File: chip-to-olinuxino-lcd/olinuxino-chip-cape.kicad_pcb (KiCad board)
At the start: 2 copper layers, 41.9 x 64.8 mm, 4 parts, among them U1 LCD Olinuxino Connector, U13 LCD Connector, U14 Generic Connector

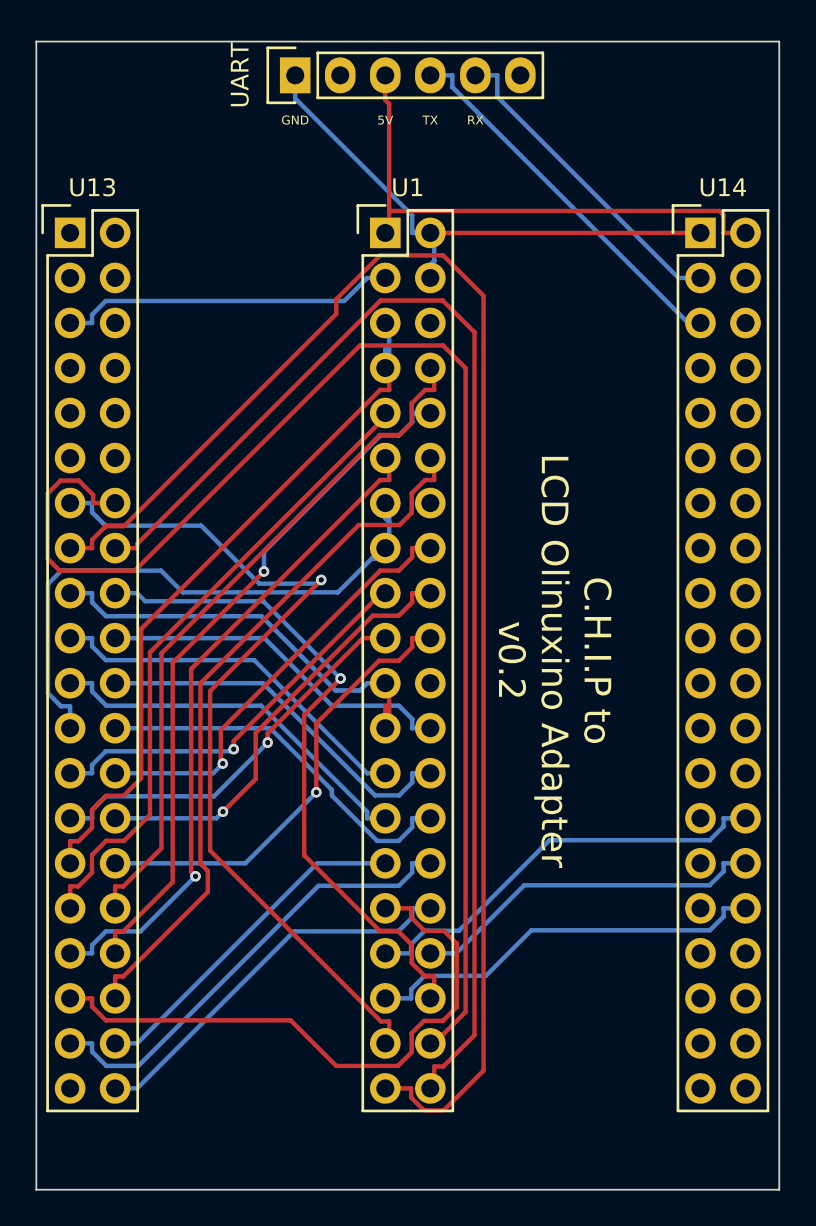
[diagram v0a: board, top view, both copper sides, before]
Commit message: rerouting
Signed-off-by: Maxime Ripard <maxime.ripard@free-electrons.com>
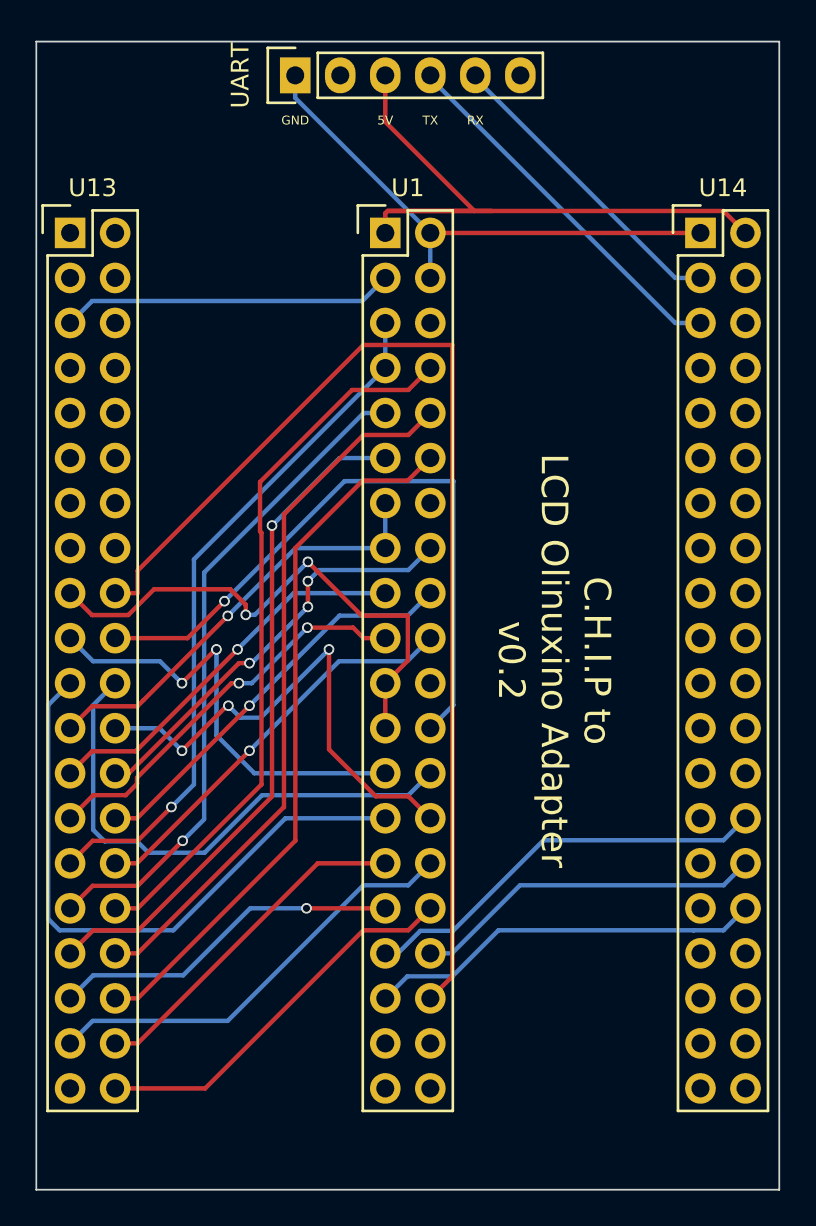
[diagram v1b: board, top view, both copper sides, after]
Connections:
- net /TPX1 renamed /TP_X-
- net /TPX2 renamed /TP_X+
- net /TPY1 renamed /TP_Y-
- net /TPY2 renamed /TP_Y+
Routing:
- net /TP_Y-: track 82.9 -> 0.22 mm
- net /TP_X+: track 78.0 -> 0.00 mm
- net /TP_Y+: track 71.5 -> 1.33 mm
- net /TP_X-: track 50.3 -> 1.76 mm, vias 1 -> 0
- net /PWM0: track 38.3 -> 64.3 mm, vias 1 -> 0
- net /LCD_D3: track 20.4 -> 37.4 mm, vias 0 -> 1
- net /LCD_CLK: track 34.4 -> 19.9 mm, vias 0 -> 1
- net /LCD_D6: track 21.6 -> 35.9 mm
- net /LCD_D10: track 34.9 -> 24.5 mm, vias 0 -> 1
- net /LCD_D5: track 21.4 -> 30.4 mm
- net /5V: track 30.9 -> 39.0 mm
- net /LCD_D7: track 21.7 -> 28.7 mm, vias 0 -> 3
- net /LCD_D2: track 25.0 -> 30.9 mm, vias 0 -> 2
- net /LCD_D4: track 21.4 -> 25.6 mm, vias 0 -> 2
- net /LCD_D15: track 25.8 -> 23.3 mm
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
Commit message: turn the connector around, and reroute
Signed-off-by: Maxime Ripard <maxime.ripard@free-electrons.com>
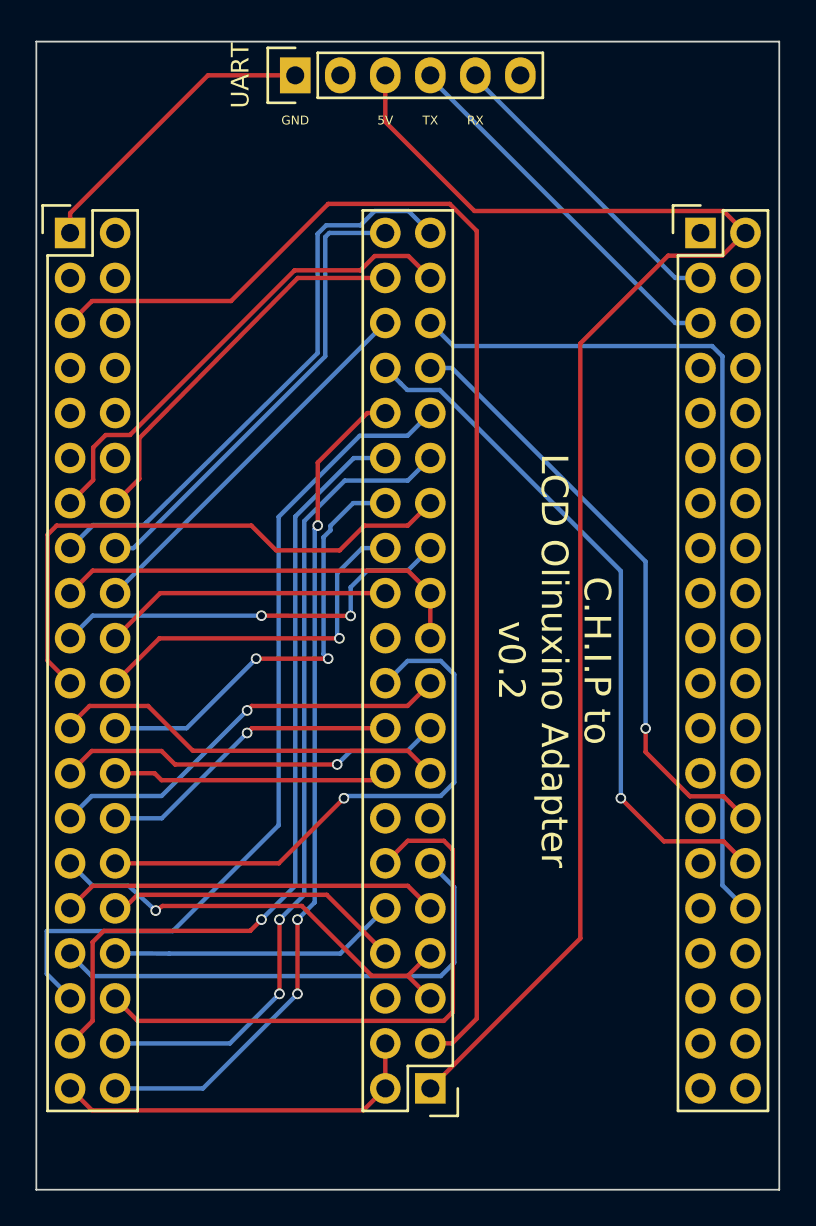
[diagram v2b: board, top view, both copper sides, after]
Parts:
- moved U1 48.3 mm to (152.3, 152.3), turned to 180 degrees
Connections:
- U1 pad 2: /GND -> /GND2
- U1 pad 4: /GND -> /GND2
- U13 pad 1: Net-(U13-Pad1) -> /GND
- U13 pad 39: Net-(U13-Pad39) -> /GND2
- U14 pad 1: /GND -> Net-(U14-Pad1)
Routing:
- net /3.3V: track 19.1 -> 74.0 mm
- net /5V: track 39.0 -> 83.0 mm
- net /PWM0: track 64.3 -> 21.6 mm
- net /TP_Y-: track 0.22 -> 33.5 mm
- net /LCD_CLK: track 19.9 -> 48.3 mm, vias 1 -> 0
- net /LCD_HSYNC: track 19.7 -> 46.8 mm, vias 0 -> 2
- net /TP_Y+: track 1.33 -> 28.2 mm
- net /TP_X-: track 1.76 -> 28.5 mm
- net /LCD_PWR: track 22.4 -> 48.9 mm
- net /LCD_DE: track 22.9 -> 47.9 mm, vias 0 -> 3
- net /LCD_D21: track 40.3 -> 16.3 mm
- net /LCD_D19: track 40.9 -> 17.6 mm
- net /TP_X+: track 0.00 -> 22.2 mm
- net /LCD_VSYNC: track 24.7 -> 46.3 mm, vias 0 -> 1
- net /GND2: track 0.00 -> 21.3 mm
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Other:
- net class Default: clearance 0.25 -> 0.1524; trace_width 0.25 -> 0.1524; via_dia 0.6 -> 0.635; via_drill 0.4 -> 0.3302
- rule trace_clearance: 0.25 -> 0.1524
- rule trace_min: 0.25 -> 0.1524
- rule via_min_drill: 0.3 -> 0.3302
- rule via_min_size: 0.4 -> 0.635
